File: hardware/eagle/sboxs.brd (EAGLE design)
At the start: 39.4 x 58.4 mm, 30 parts

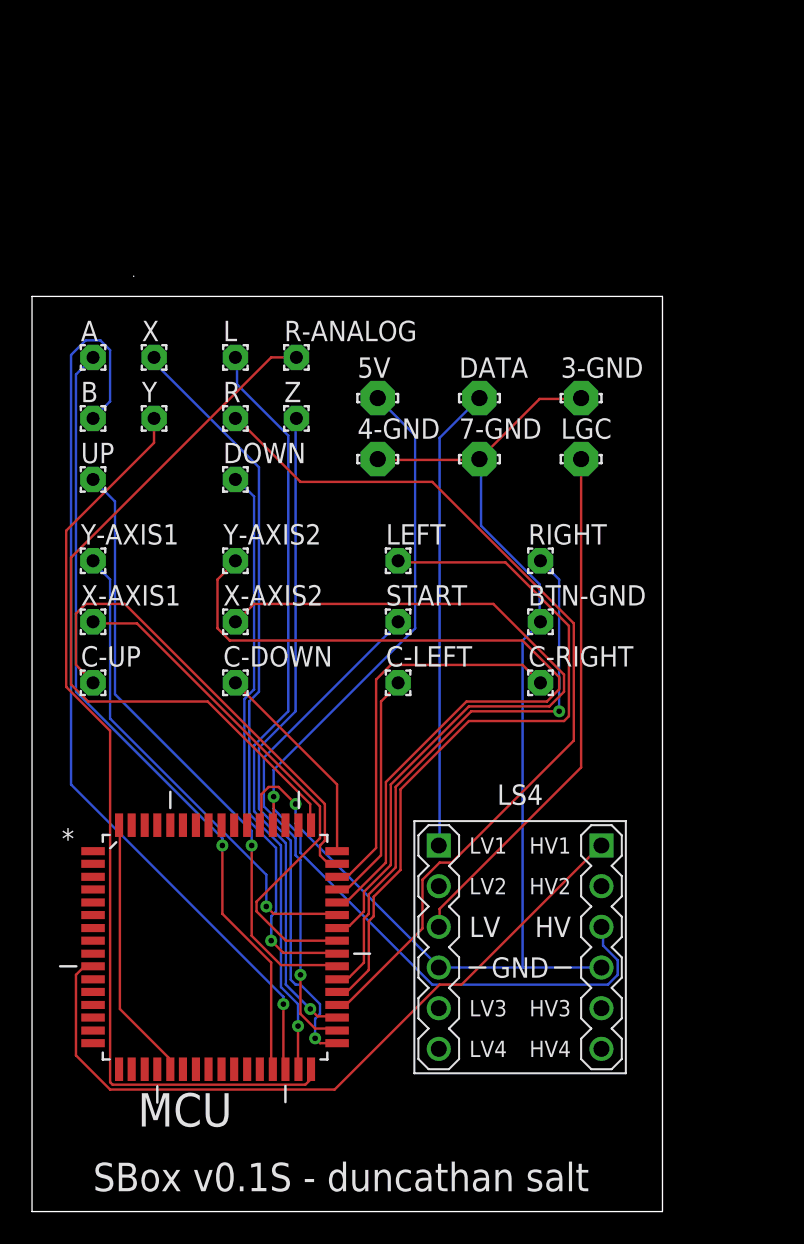
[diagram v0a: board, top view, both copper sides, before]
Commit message: update to small pcb v0.2 and minor changes to overall schematic
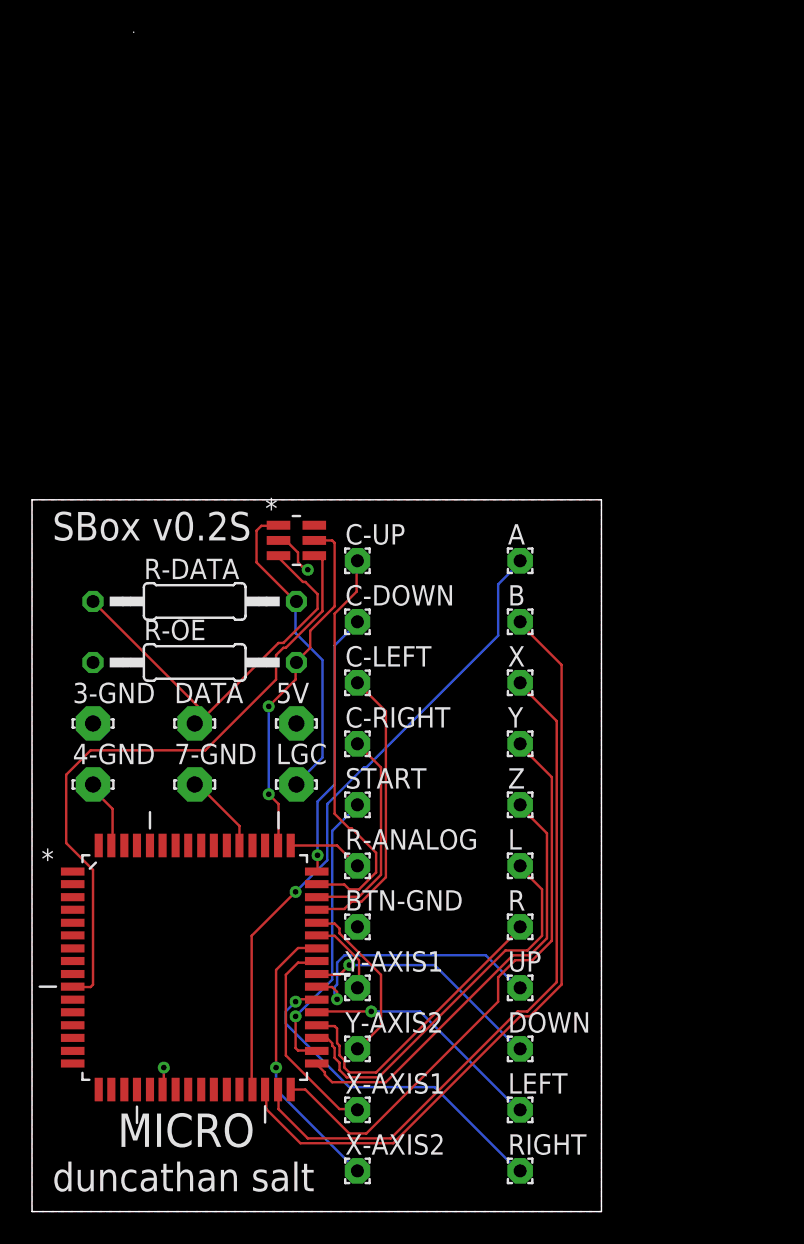
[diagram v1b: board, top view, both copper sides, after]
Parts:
- removed LS4: LEVEL-SHIFTER-4CH, diy-modules:LEVEL-SHIFTER-4CH
- removed MCU: ATMEGA1281-16AU, Atmel_By_element14_Batch_1-00:QFP80P1600X1600X120-64N
- added MICRO: ATMEGA1281-16AU, Atmel_By_element14_Batch_1-00:QFP80P1600X1600X120-64N
- added R-DATA: 1 kΩ, resistor:0207/12
- added R-OE: 200 Ω, resistor:0207/12
- added TTL: TXS0101_DBV_6, txs0101:DBV6
- moved UP 41.5 mm to (30.5, 14.0)
- moved DOWN 39.8 mm to (30.5, 10.2)
- moved RIGHT 38.1 mm to (30.5, 2.54)
- moved 3-GND 36.6 mm to (3.81, 30.5)
- moved L 36.4 mm to (30.5, 21.6)
- moved R 36.4 mm to (30.5, 17.8)
- moved LEFT 35.1 mm to (30.5, 6.35)
- moved X-AXIS2 35.1 mm to (20.3, 2.54)
- moved X-AXIS1 34.7 mm to (20.3, 6.35)
- moved R-ANALOG 32.0 mm to (20.3, 21.6)
- moved Y-AXIS2 31.4 mm to (20.3, 10.2)
- moved Y-AXIS1 31.4 mm to (20.3, 14.0)
- moved X 30.6 mm to (30.5, 33.0)
- moved Y 30.6 mm to (30.5, 29.2)
- moved A 29.5 mm to (30.5, 40.6)
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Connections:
- removed net N$21: LS4.J2.1, MCU.10
- removed net N$23: MCU.21, MCU.64
- removed net N$25: 5V.MP, LS4.J2.3, MCU.52
- removed net N$26: LGC.MP, LS4.J1.3
- removed net N$27: 3-GND.MP, 4-GND.MP, 7-GND.MP, BTN-GND.1, LS4.J1.4, LS4.J2.4, MCU.53
- new net +3V3: LGC.MP, R-DATA.2, TTL.1
- new net +5V: 5V.MP, MICRO.21, MICRO.52, MICRO.64, TTL.6
- new net AGND: 3-GND.MP, 4-GND.MP, 7-GND.MP, BTN-GND.1, MICRO.22, MICRO.53, MICRO.63, R-OE.1, TTL.2
- new net N$29: MICRO.10, TTL.4
- new net N$30: MICRO.50, R-OE.2, TTL.5
- net N$1: now also MICRO.32; no longer MCU.32
- net N$10: now also MICRO.38; no longer MCU.38
- net N$11: now also MICRO.39; no longer MCU.39
- net N$12: now also MICRO.40; no longer MCU.40
- net N$13: now also MICRO.41; no longer MCU.41
- net N$14: now also MICRO.42; no longer MCU.42
- net N$15: now also MICRO.44; no longer MCU.44
- net N$16: now also MICRO.45; no longer MCU.45
- net N$17: now also MICRO.46; no longer MCU.46
- net N$18: now also MICRO.47; no longer MCU.47
- net N$19: now also MICRO.48; no longer MCU.48
- net N$2: now also MICRO.31; no longer MCU.31
- net N$20: now also MICRO.49; no longer MCU.49
- net N$24: now also MICRO.43; no longer MCU.43
- net N$28: now also R-DATA.1, TTL.3; no longer LS4.J1.1
- net N$3: now also MICRO.30; no longer MCU.30
- net N$4: now also MICRO.29; no longer MCU.29
- net N$5: now also MICRO.33; no longer MCU.33
- net N$6: now also MICRO.34; no longer MCU.34
- net N$7: now also MICRO.35; no longer MCU.35
- net N$8: now also MICRO.36; no longer MCU.36
- net N$9: now also MICRO.37; no longer MCU.37
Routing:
- net N$27: track 77.0 -> 0.00 mm, vias 1 -> 0
- net N$25: track 62.4 -> 0.00 mm, vias 1 -> 0
- net N$21: track 46.4 -> 0.00 mm
- net N$20: track 46.5 -> 4.69 mm
- net N$29: track 0.00 -> 40.1 mm
- net N$15: track 50.4 -> 10.8 mm
- net N$8: track 57.2 -> 18.9 mm
- net N$26: track 32.9 -> 0.00 mm
- net N$14: track 47.9 -> 17.8 mm, vias 0 -> 1
- net N$9: track 45.1 -> 15.4 mm, vias 0 -> 1
- net N$24: track 30.8 -> 5.07 mm, vias 1 -> 0
- net N$30: track 0.00 -> 22.3 mm, vias 0 -> 2
- net N$7: track 46.4 -> 24.4 mm, vias 1 -> 0
- net N$11: track 38.8 -> 16.9 mm
- net N$1: track 58.2 -> 36.4 mm
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- added copper zone on layer 1, net +5V
- added copper zone on layer 16, net AGND
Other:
- board size 39.4 x 58.4 mm -> 35.6 x 73.7 mm
- board text added: "SBox v0.2S"
- board text added: "duncathan salt"
- board text removed: "SBox v0.1S - duncathan salt"
